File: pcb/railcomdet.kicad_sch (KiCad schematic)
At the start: 43 parts, among them J1 MVE252-5-V, J10 MVE252-5-V, J2 MVE252-5-V, J3 MVE252-5-V, J4 MVE252-5-V, J5 MVE252-5-V, J9 MVE252-5-V, U1 VO0631T, U2 VO0631T, U3 VO0631T

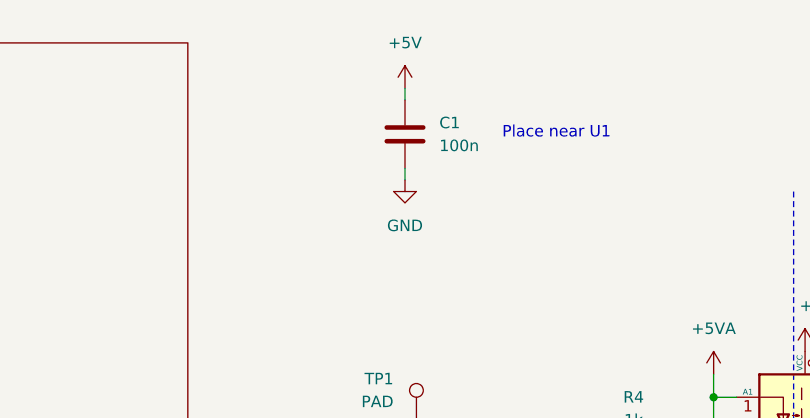
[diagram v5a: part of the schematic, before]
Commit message: pcb: wire multiplexer's inputs.
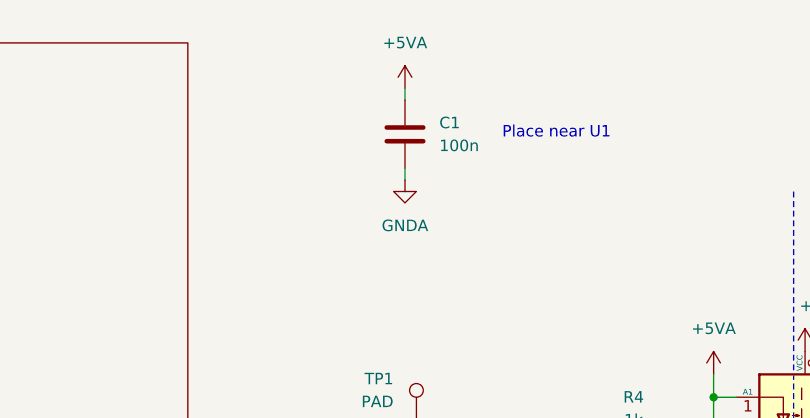
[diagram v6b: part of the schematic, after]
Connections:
- net +5V: no longer C1.1
- net +5VA: now also C1.1
- net GND: no longer C1.2
- net GNDA: now also C1.2
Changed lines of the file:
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@@
+    )
+  )
+  (symbol (lib_id "power:GNDA") (at 101.6 31.75 0) (unit 1)
+    (in_bom yes) (on_board yes) (dnp no)
+    (property "Reference" "#PWR02" (at 101.6 38.1 0)
+      (effects (font (size 1.27 1.27)) hide)
+    )
+    (property "Value" "GNDA" (at 101.6 36.83 0)
+      (effects (font (size 1.27 1.27)))
+    )
+    (property "Footprint" "" (at 101.6 31.75 0)
+      (effects (font (size 1.27 1.27)) hide)
+    )
+    (property "Datasheet" "" (at 101.6 31.75 0)
+      (effects (font (size 1.27 1.27)) hide)
+    )
+    (pin "1")
+    (instances
+      (project "railcomdet"
+        (path "/3e59d29f-2657-4552-9290-3c54fadfdf63"
+          (reference "#PWR02") (unit 1)
+        )
+      )
     )
   )
@@
     )
   )
-  (symbol (lib_id "power:GND") (at 101.6 31.75 0) (unit 1)
-    (in_bom yes) (on_board yes) (dnp no) (fields_autoplaced)
-    (property "Reference" "#PWR02" (at 101.6 38.1 0)
-      (effects (font (size 1.27 1.27)) hide)
-    )
-    (property "Value" "GND" (at 101.6 36.83 0)
-      (effects (font (size 1.27 1.27)))
-    )
-    (property "Footprint" "" (at 101.6 31.75 0)
-      (effects (font (size 1.27 1.27)) hide)
-    )
-    (property "Datasheet" "" (at 101.6 31.75 0)
-      (effects (font (size 1.27 1.27)) hide)
-    )
-    (pin "1")
-    (instances
-      (project "railcomdet"
-        (path "/3e59d29f-2657-4552-9290-3c54fadfdf63"
-          (reference "#PWR02") (unit 1)
-        )
-      )
-    )
-  )
   (symbol (lib_id "Device:R") (at 127 96.52 0) (mirror y) (unit 1)
     (in_bom yes) (on_board yes) (dnp no) (fields_autoplaced)
@@
     )
   )
+  (symbol (lib_id "power:+5VA") (at 101.6 21.59 0) (unit 1)
+    (in_bom yes) (on_board yes) (dnp no)
+    (property "Reference" "#PWR01" (at 101.6 25.4 0)
+      (effects (font (size 1.27 1.27)) hide)
+    )
+    (property "Value" "+5VA" (at 101.6 16.51 0)
+      (effects (font (size 1.27 1.27)))
+    )
+    (property "Footprint" "" (at 101.6 21.59 0)
+      (effects (font (size 1.27 1.27)) hide)
+    )
+    (property "Datasheet" "" (at 101.6 21.59 0)
+      (effects (font (size 1.27 1.27)) hide)
+    )
+    (pin "1")
+    (instances
+      (project "railcomdet"
+        (path "/3e59d29f-2657-4552-9290-3c54fadfdf63"
+          (reference "#PWR01") (unit 1)
+        )
+      )
+    )
+  )
   (symbol (lib_id "power:+3V3") (at 153.67 96.52 0) (unit 1)
     (in_bom yes) (on_board yes) (dnp no) (fields_autoplaced)
@@
         )
       )
-    )
-  )
-  (symbol (lib_id "power:+5V") (at 101.6 21.59 0) (unit 1)
-    (in_bom yes) (on_board yes) (dnp no) (fields_autoplaced)
-    (property "Reference" "#PWR01" (at 101.6 25.4 0)
-      (effects (font (size 1.27 1.27)) hide)
-    )
-    (property "Value" "+5V" (at 101.6 16.51 0)
-      (effects (font (size 1.27 1.27)))
-    )
-    (property "Footprint" "" (at 101.6 21.59 0)
-      (effects (font (size 1.27 1.27)) hide)
-    )
-    (property "Datasheet" "" (at 101.6 21.59 0)
-      (effects (font (size 1.27 1.27)) hide)
-    )
-    (pin "1")
-    (instances
-      (project "railcomdet"
-        (path "/3e59d29f-2657-4552-9290-3c54fadfdf63"
-          (reference "#PWR01") (unit 1)
-        )
-      )

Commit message: pcb: use THT testpins for DCC part.
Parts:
- TP1, TP2, TP3, TP4, TP5, TP6: footprint TestPoint:TestPoint_Pad_D2.0mm -> Connector_PinHeader_2.54mm:PinHeader_1x01_P2.54mm_Vertical
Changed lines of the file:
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@@
       (effects (font (size 1.27 1.27)) (justify left))
     )
-    (property "Footprint" "TestPoint:TestPoint_Pad_D2.0mm" (at 97.79 139.7 0)
+    (property "Footprint" "Connector_PinHeader_2.54mm:PinHeader_1x01_P2.54mm_Vertical" (at 97.79 139.7 0)
       (effects (font (size 1.27 1.27)) hide)
     )
@@
       (effects (font (size 1.27 1.27)) (justify left))
     )
-    (property "Footprint" "TestPoint:TestPoint_Pad_D2.0mm" (at 97.79 58.42 0)
+    (property "Footprint" "Connector_PinHeader_2.54mm:PinHeader_1x01_P2.54mm_Vertical" (at 97.79 58.42 0)
       (effects (font (size 1.27 1.27)) hide)
     )
@@
       (effects (font (size 1.27 1.27)) (justify left))
     )
-    (property "Footprint" "TestPoint:TestPoint_Pad_D2.0mm" (at 97.79 99.06 0)
+    (property "Footprint" "Connector_PinHeader_2.54mm:PinHeader_1x01_P2.54mm_Vertical" (at 97.79 99.06 0)
       (effects (font (size 1.27 1.27)) hide)
     )
@@
       (effects (font (size 1.27 1.27)) (justify left))
     )
-    (property "Footprint" "TestPoint:TestPoint_Pad_D2.0mm" (at 97.79 68.58 0)
+    (property "Footprint" "Connector_PinHeader_2.54mm:PinHeader_1x01_P2.54mm_Vertical" (at 97.79 68.58 0)
       (effects (font (size 1.27 1.27)) hide)
     )
@@
       (effects (font (size 1.27 1.27)) (justify left))
     )
-    (property "Footprint" "TestPoint:TestPoint_Pad_D2.0mm" (at 97.79 149.86 0)
+    (property "Footprint" "Connector_PinHeader_2.54mm:PinHeader_1x01_P2.54mm_Vertical" (at 97.79 149.86 0)
       (effects (font (size 1.27 1.27)) hide)
     )
@@
       (effects (font (size 1.27 1.27)) (justify right))
     )
-    (property "Footprint" "TestPoint:TestPoint_Pad_D2.0mm" (at 107.95 109.22 0)
-      (effects (font (size 1.27 1.27)) hide)
-    )
+    (property "Footprint" "Connector_PinHeader_2.54mm:PinHeader_1x01_P2.54mm_Vertical" (at 107.95 109.22 0)
+      (effects (font (size 1.27 1.27)) hide)
+    )

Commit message: pcb: everything routed.
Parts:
- TP10, TP11, TP12, TP7, TP8, TP9: footprint TestPoint:TestPoint_Pad_D2.0mm -> Connector_PinHeader_2.54mm:PinHeader_1x01_P2.54mm_Vertical
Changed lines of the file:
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@@
       (effects (font (size 1.27 1.27)) (justify left))
     )
-    (property "Footprint" "TestPoint:TestPoint_Pad_D2.0mm" (at 208.28 137.16 0)
+    (property "Footprint" "Connector_PinHeader_2.54mm:PinHeader_1x01_P2.54mm_Vertical" (at 208.28 137.16 0)
       (effects (font (size 1.27 1.27)) hide)
     )
@@
       (effects (font (size 1.27 1.27)) (justify left))
     )
-    (property "Footprint" "TestPoint:TestPoint_Pad_D2.0mm" (at 208.28 152.4 0)
+    (property "Footprint" "Connector_PinHeader_2.54mm:PinHeader_1x01_P2.54mm_Vertical" (at 208.28 152.4 0)
       (effects (font (size 1.27 1.27)) hide)
     )
@@
       (effects (font (size 1.27 1.27)) (justify left))
     )
-    (property "Footprint" "TestPoint:TestPoint_Pad_D2.0mm" (at 208.28 71.12 0)
+    (property "Footprint" "Connector_PinHeader_2.54mm:PinHeader_1x01_P2.54mm_Vertical" (at 208.28 71.12 0)
       (effects (font (size 1.27 1.27)) hide)
     )
@@
       (effects (font (size 1.27 1.27)) (justify left))
     )
-    (property "Footprint" "TestPoint:TestPoint_Pad_D2.0mm" (at 208.28 101.6 0)
+    (property "Footprint" "Connector_PinHeader_2.54mm:PinHeader_1x01_P2.54mm_Vertical" (at 208.28 101.6 0)
       (effects (font (size 1.27 1.27)) hide)
     )
@@
       (effects (font (size 1.27 1.27)) (justify left))
     )
-    (property "Footprint" "TestPoint:TestPoint_Pad_D2.0mm" (at 208.28 55.88 0)
+    (property "Footprint" "Connector_PinHeader_2.54mm:PinHeader_1x01_P2.54mm_Vertical" (at 208.28 55.88 0)
       (effects (font (size 1.27 1.27)) hide)
     )
@@
       (effects (font (size 1.27 1.27)) (justify left))
     )
-    (property "Footprint" "TestPoint:TestPoint_Pad_D2.0mm" (at 208.28 111.76 0)
-      (effects (font (size 1.27 1.27)) hide)
-    )
+    (property "Footprint" "Connector_PinHeader_2.54mm:PinHeader_1x01_P2.54mm_Vertical" (at 208.28 111.76 0)
+      (effects (font (size 1.27 1.27)) hide)
+    )
